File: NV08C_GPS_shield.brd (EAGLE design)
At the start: 99.1 x 53.3 mm, 65 parts, among them IC1 MCP1702-3.3, IC2 74LVC1T45SOT23-HAND, IC3 74LVC1T45SOT23-HAND, IC4 74LVC1T45SOT23-HAND, IC5 74LVC1T45SOT23-HAND, IC6 74LVC1T45SOT23-HAND, IC7 74LVC1T45SOT23-HAND, X1 MEGA2560, X2 CONN-SMATHD-SMD-EDGE, X4 UFL

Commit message: Minor layout changes.
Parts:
- X2: value CONN-SMATHD-SMD-EDGE -> CONN-SMATHD; device SteveMarple:SMA-THD-EDGE -> SteveMarple:SMA-THD
- moved C2 2.54 mm to (5.08, 36.8), turned to 180 degrees
- moved X2 1.27 mm to (5.08, 45.7)
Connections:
- net GND: no longer X2.GND@EDGE0, X2.GND@EDGE1, X2.GND@EDGE2, X2.GND@EDGE3
- net N$4: no longer X2.SIG@EDGE
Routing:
- net V_ANT: track 30.3 -> 66.4 mm
- net IOREF: track 215.7 -> 196.4 mm
- net VBATT: track 47.0 -> 59.5 mm
- net +5V: track 193.8 -> 200.5 mm
- net GND: track 448.9 -> 444.9 mm, vias 4 -> 36
- net MOSI: track 90.5 -> 87.5 mm
- net N$4: track 22.1 -> 24.6 mm
- net SCK: track 103.9 -> 101.8 mm

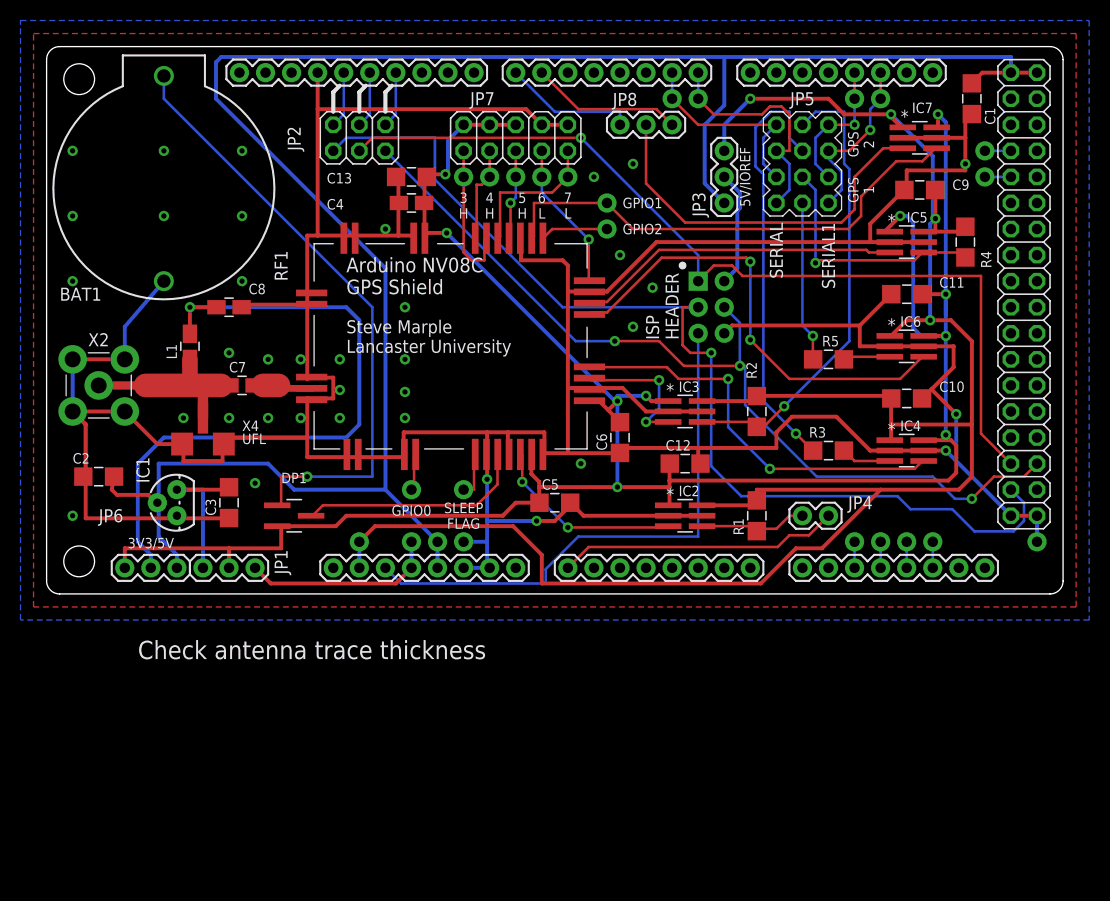
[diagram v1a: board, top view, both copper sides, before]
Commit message: Adjusting position of NV08C GPS module and some other components.
NV08C moved 0.1" left.
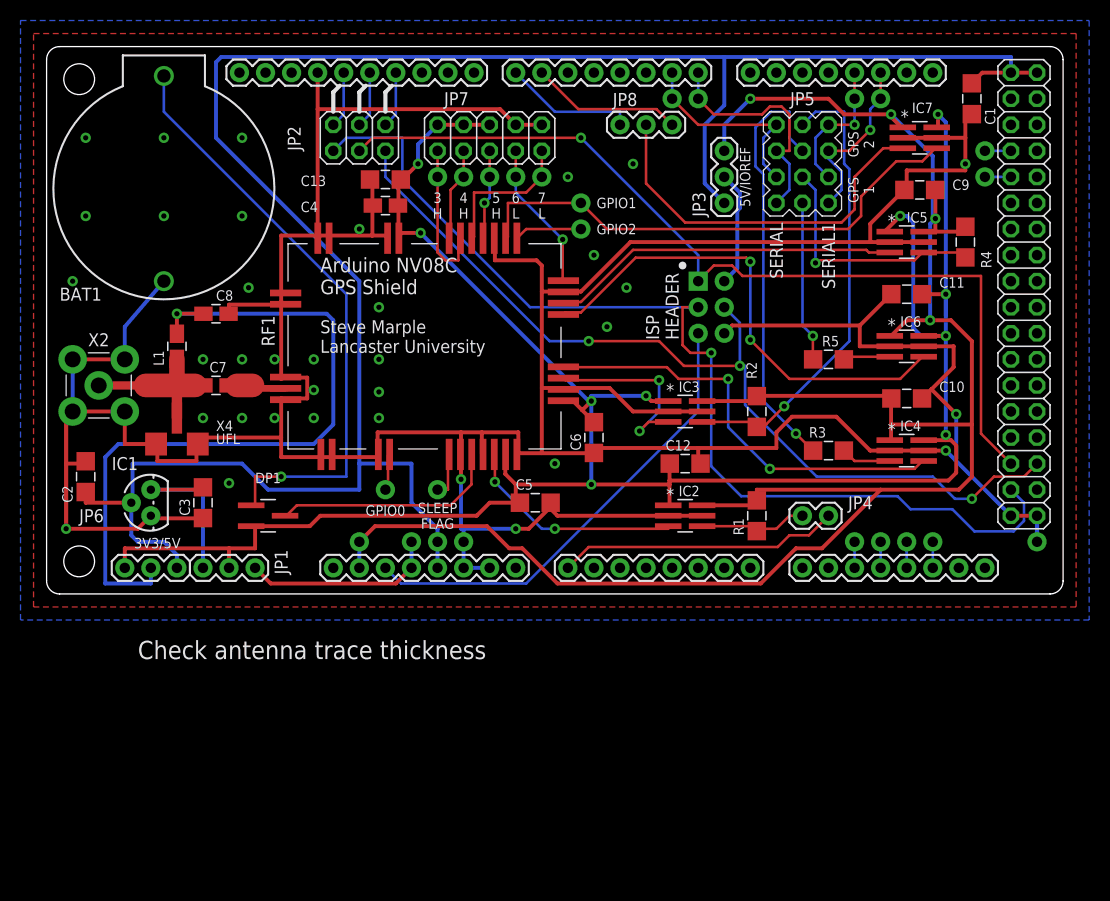
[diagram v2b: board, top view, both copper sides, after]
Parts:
- moved C13 2.55 mm to (33.0, 65.8)
- moved C4 2.55 mm to (33.0, 63.2)
- moved C3 2.54 mm to (15.2, 34.3)
- moved X4 2.54 mm to (12.7, 40.0)
- moved C6 2.54 mm to (53.3, 40.6)
- moved C7 2.54 mm to (16.5, 45.7)
- moved DP1 2.54 mm to (21.6, 33.0)
- moved IC1 2.54 mm to (10.2, 34.3)
- moved JP7 2.54 mm to (43.2, 69.8)
- moved RF1 2.54 mm to (36.8, 49.5)
- moved U$10 2.54 mm to (52.1, 61.0)
- moved U$11 2.54 mm to (38.1, 66.0)
- moved U$12 2.54 mm to (40.6, 66.0)
- moved U$13 2.54 mm to (43.2, 66.0)
- moved U$14 2.54 mm to (45.7, 66.0)
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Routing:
- net GND: track 444.9 -> 453.8 mm, vias 36 -> 35
- net N$4: track 24.6 -> 16.0 mm
- net !RESET: track 53.6 -> 45.7 mm
- net +5V: track 200.5 -> 207.8 mm
- net V_ANT: track 66.4 -> 72.2 mm
- net GPS_RX2: track 13.6 -> 18.3 mm
- net +3V3: track 225.8 -> 228.8 mm
- net !GPS_RESET: track 19.0 -> 21.7 mm
- net GPS_TX2: track 39.7 -> 42.3 mm
- net GPIO1: track 48.2 -> 50.8 mm
- net GPS_TX1: track 45.1 -> 47.7 mm
- net N$1: track 15.5 -> 18.0 mm
- net GPS_RX1: track 31.5 -> 34.0 mm
- net IOREF: track 196.4 -> 194.8 mm
- net MOSI: track 87.5 -> 89.0 mm
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
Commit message: Minor changes to improve SCK routing and GND fill.
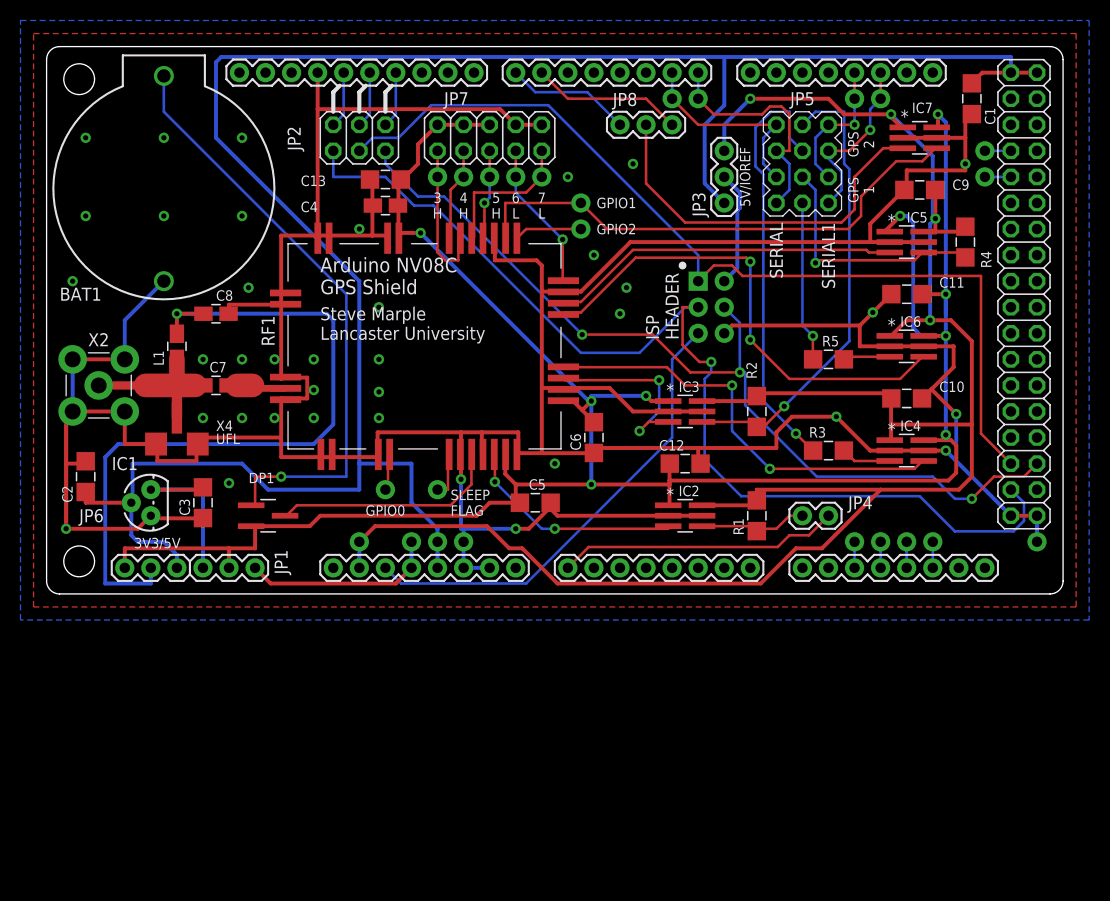
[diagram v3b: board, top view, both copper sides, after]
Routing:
- net MISO: track 88.9 -> 91.6 mm, vias 1 -> 0
- net SCK: track 101.8 -> 103.5 mm
- net 7: track 13.0 -> 12.3 mm
- net GND: track 453.8 -> 454.0 mm, vias 35 -> 37
- net +3V3: vias 10 -> 9
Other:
- board text removed: "Check antenna trace thickness"

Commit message: Minor layout changes.
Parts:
- C10, C11: value 100n -> 1u
- C12, C9: value 100n -> 22p; device SteveMarple:1206-HAND -> SteveMarple:0805-HAND
- C13: value 1u -> 22p; device SteveMarple:1206-HAND -> SteveMarple:0805-HAND
- C3, C5, C6: value 1u -> 100n
- C4: value 22p -> 100n; device SteveMarple:0805-HAND -> SteveMarple:1206-HAND
- C7, C8: value 22p -> 1u; device SteveMarple:0805-HAND -> SteveMarple:1206-HAND
- U$10: value ? -> PAD
- U$11: value PAD -> CALUNIUM-SHIELD-V3V3-NO-HOLES-NO-TEXT; device SteveMarple:PAD -> SteveMarple:CALUNIUM-SHIELD-NO-OUTLINE-NO-HOLES-NO-TEXT-V3
- U$20: value PAD -> ?
- U$5: value CALUNIUM-SHIELD-V3V3-NO-HOLES-NO-TEXT -> PAD; device SteveMarple:CALUNIUM-SHIELD-NO-OUTLINE-NO-HOLES-NO-TEXT-V3 -> SteveMarple:PAD
- moved C1 93.9 mm to (3.81, 36.8), turned to 90 degrees
- moved C7 78.8 mm to (90.2, 73.7), turned to 270 degrees
- moved C3 76.2 mm to (85.1, 64.8), turned to 180 degrees
- moved U$25 59.9 mm to (48.3, 66.0), turned to 270 degrees
- moved U$17 58.4 mm to (96.5, 30.5)
- moved U$21 55.9 mm to (38.1, 66.0)
- moved U$6 55.9 mm to (86.4, 30.5), turned to 270 degrees
- moved C4 54.2 mm to (83.8, 44.5), turned to 0 degrees
- moved U$22 52.1 mm to (40.6, 66.0)
- moved C9 52.1 mm to (33.0, 63.2)
- moved U$1 50.1 mm to (38.1, 30.5)
- moved U$2 50.1 mm to (35.6, 30.5)
- moved U$23 48.3 mm to (43.2, 66.0), turned to 270 degrees
- moved U$19 47.6 mm to (52.1, 63.5)
- moved U$8 47.2 mm to (61.0, 73.7), turned to 0 degrees
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- renumbered X4 to X3
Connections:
- net !RESET: now also U$11.!ISP_RESET, U$11.!RESET@0; no longer U$5.!ISP_RESET, U$5.!RESET@0
- net +3V3: now also C10.1, C8.1, C9.1; no longer C12.1, C13.1, C4.1
- net +5V: now also C7.1, U$1.1, U$11.5V; no longer C2.1, U$17.1, U$5.5V
- net 11: now also U$11.11@0; no longer U$5.11@0
- net 12: now also U$11.12@0; no longer U$5.12@0
- net 13: now also U$11.13@0; no longer U$5.13@0
- net 3V3_SHIELD: now also U$11.3.3V, U$2.1; no longer U$16.1, U$5.3.3V
- net 6: now also U$11.6; no longer U$5.6
- net 7: now also U$11.7; no longer U$5.7
- net A0: now also U$11.A0; no longer U$5.A0
- net GND: now also C7.2, U$11.GND@0, U$11.GND@1, U$11.GND@2, U$11.GND@3, U$12.1, U$17.1; no longer C12.2, U$18.1, U$25.1, U$5.GND@0, U$5.GND@1, U$5.GND@2, U$5.GND@3
- net GPIO0: now also U$18.1; no longer U$8.1
- net GPIO1: now also U$19.1; no longer U$9.1
- net GPIO2: now also U$20.1; no longer U$10.1
- net GPIO3: now also U$21.1; no longer U$11.1
- net GPIO4: now also U$22.1; no longer U$12.1
- net GPIO5: now also U$23.1; no longer U$13.1
- net GPIO6: now also U$24.1; no longer U$14.1
- net GPIO7: now also U$25.1; no longer U$15.1
- net IOREF: now also C3.1, C4.1, U$11.IOREF, U$13.1; no longer C10.1, C9.1, U$5.IOREF, U$6.1
- net ISP_VCC: now also U$11.ISP_VCC; no longer U$5.ISP_VCC
- net MEGA_28: now also U$14.1; no longer U$24.1
- net MEGA_30: now also U$15.1; no longer U$23.1
- net MISO: now also U$11.ISP_MISO; no longer U$5.ISP_MISO
- net MOSI: now also U$11.ISP_MOSI; no longer U$5.ISP_MOSI
- net N$1: now also C2.1; no longer C3.1
- net N$10: now also U$11.16, U$3.1; no longer U$22.1, U$5.16
- net N$2: now also U$11.19, U$6.1; no longer U$19.1, U$5.19
- net N$4: now also C12.2; no longer C7.2
- net N$6: now also U$11.18, U$5.1; no longer U$20.1, U$5.18
- net N$7: now also C12.1; no longer C7.1
- net N$9: now also U$11.17, U$4.1; no longer U$21.1, U$5.17
- net RX0: now also U$11.0(RX0), U$7.1; no longer U$1.1, U$5.0(RX0)
- net RX1: now also U$11.2@1, U$9.1; no longer U$3.1, U$5.2@1
- net SCK: now also U$11.ISP_SCK; no longer U$5.ISP_SCK
- net SLEEP_FLAG: now also U$16.1; no longer U$7.1
- net TX0: now also U$11.1(TX0), U$8.1; no longer U$2.1, U$5.1(TX0)
- net TX1: now also U$10.1, U$11.3@1; no longer U$4.1, U$5.3@1
- net V_ANT: now also C13.1; no longer C8.1
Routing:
- net GND: track 454.0 -> 451.7 mm
- net V_ANT: track 72.2 -> 73.1 mm
- net RX0: track 23.7 -> 22.9 mm
- net N$4: track 16.0 -> 15.3 mm

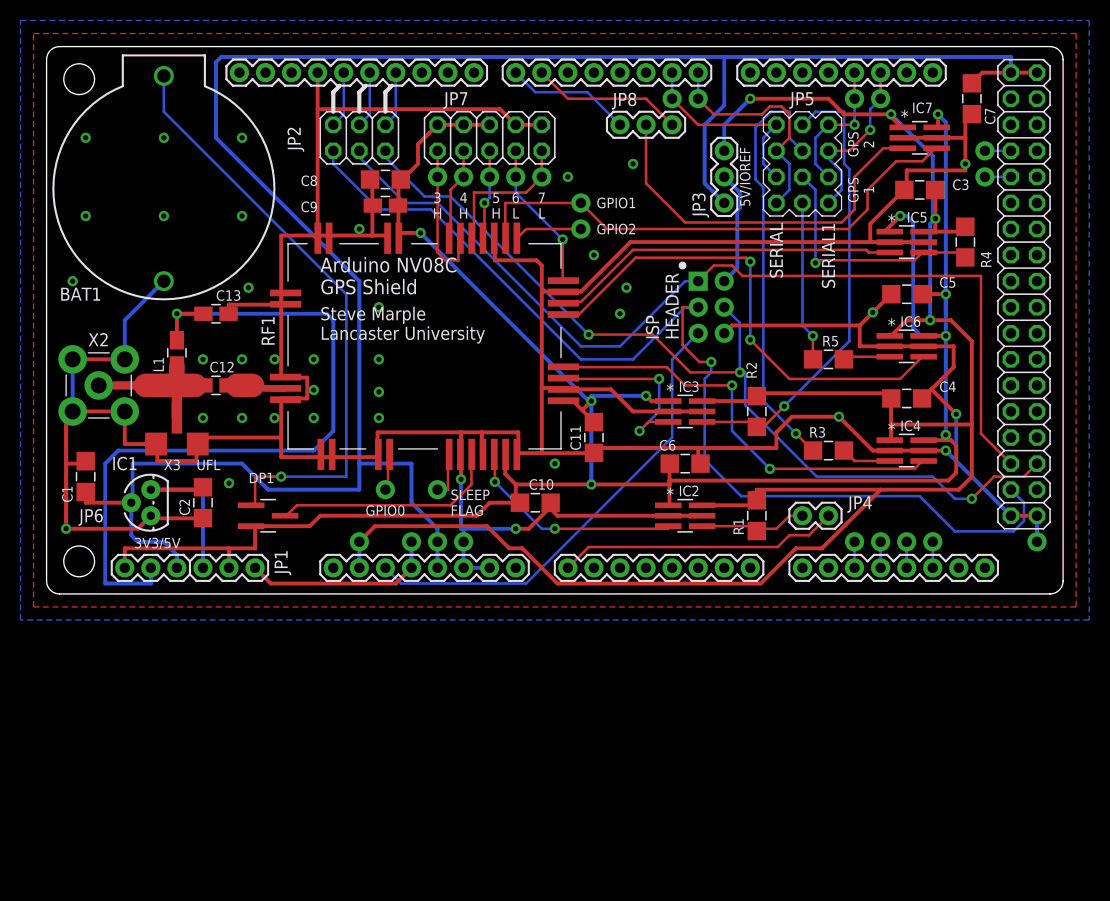
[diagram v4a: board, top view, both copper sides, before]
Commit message: Translate to (0,0). Minor silkscreen changes.
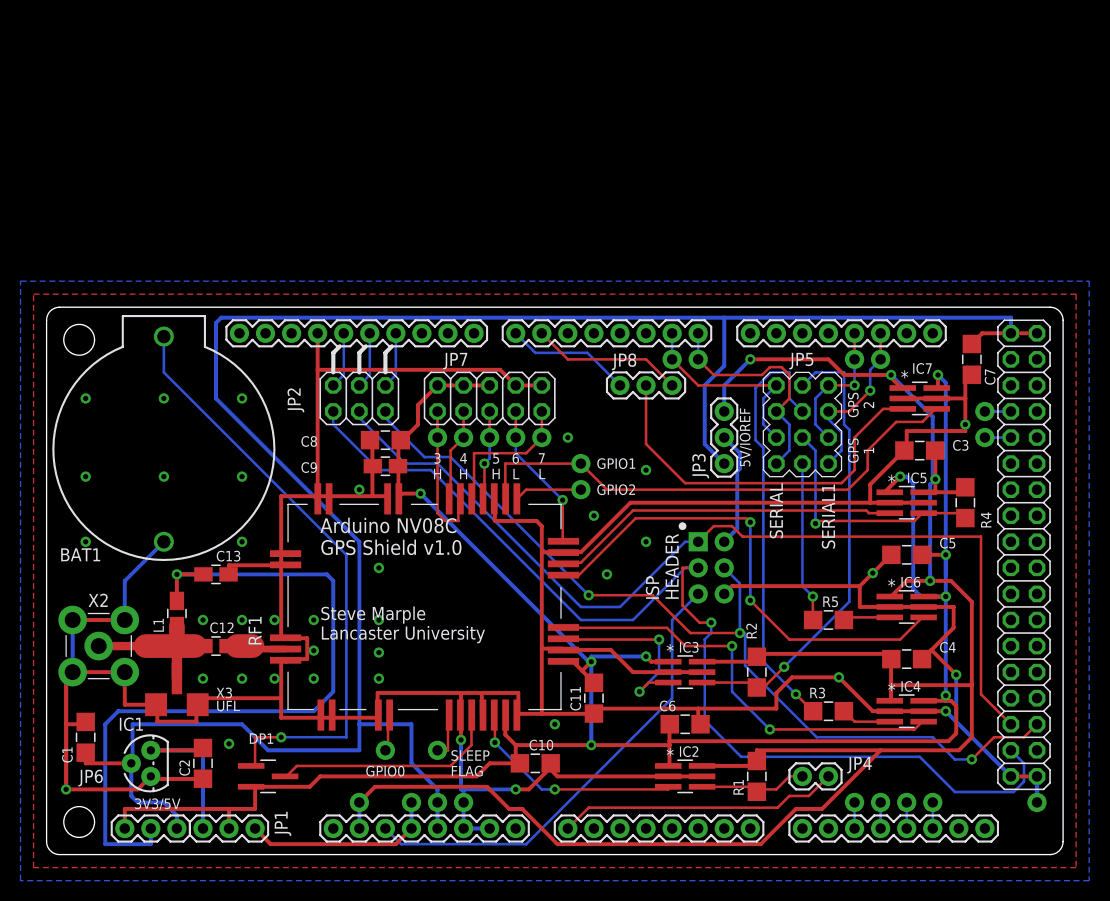
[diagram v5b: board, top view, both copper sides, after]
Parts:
- moved C9 25.4 mm to (33.0, 37.8)
- moved JP8 25.4 mm to (55.9, 45.7)
- moved U$15 25.4 mm to (91.4, 40.6)
- moved U$21 25.4 mm to (38.1, 40.6)
- moved U$22 25.4 mm to (40.6, 40.6)
- moved U$23 25.4 mm to (43.2, 40.6)
- moved U$24 25.4 mm to (45.7, 40.6)
- moved U$25 25.4 mm to (48.3, 40.6)
- moved BAT1 25.4 mm to (11.4, 30.5)
- moved C4 25.4 mm to (83.8, 19.1)
- moved C6 25.4 mm to (62.2, 12.7)
- moved DP1 25.4 mm to (21.6, 7.62)
- moved IC2 25.4 mm to (62.2, 7.62)
- moved IC6 25.4 mm to (83.8, 24.1)
- moved JP1 25.4 mm to (20.3, 2.54)
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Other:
- board text added: "Arduino NV08C GPS Shield v1.0"
- board text removed: "Arduino NV08C GPS Shield"
